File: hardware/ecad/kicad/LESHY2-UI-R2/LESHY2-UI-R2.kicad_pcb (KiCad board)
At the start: 6 copper layers, 80 x 150 mm, 432 parts, among them J1 Hirose FH34SRJ-50S-0.5SH(50), J10 Samtec FTSH-105-01-L-DV-K-P-TR, J11 GCT USB4105-GF-A, J12 GCT RFPC-SMA31-FN-175-A, J13 Hirose U.FL-R-SMT-1(80), J14 GCT RFPC-SMA31-FN-175-A, J15 Hirose U.FL-R-SMT-1(80), J16 GCT RFPC-SMA31-FN-175-A, J17 Hirose U.FL-R-SMT-1(80), J18 Hirose FX8C-80P-SV1(92), J2 Samtec FTSH-105-01-L-DV-K-P-TR, J3 GCT RFPC-SMA32-FN-175-A, J4 Hirose U.FL-R-SMT-1(80), J5 Hirose DM3AT-SF-PEJM5, J6 Samtec FTSH-105-01-L-DV-K-P-TR, J7 GCT RFPC-SMA32-FN-175-A, J8 Hirose U.FL-R-SMT-1(80), J9 GCT USB4105-GF-A, Q1 Diodes Incorporated DMN2056U-7, Q2 Diodes Incorporated 2N7002DW-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, Q3 Diodes Incorporated DMN2056U-7, Q4 Diodes Incorporated DMN2056U-7, Q5 Diodes Incorporated DMN2056U-7, Q6 Diodes Incorporated 2N7002DW-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, SW1 Alps Alpine SKRTLAE010, SW10 OMRON B3S-1100P, SW11 OMRON B3S-1100P, SW12 OMRON B3S-1100P, SW13 OMRON B3S-1100P, SW14 OMRON B3S-1100P, SW15 OMRON B3S-1100P, SW16 OMRON B3S-1100P, SW17 OMRON B3S-1100P, SW18 Alps Alpine SKRTLAE010, SW19 Alps Alpine SKRTLAE010, SW2 Alps Alpine SKRTLAE010, SW20 Alps Alpine SKRTLAE010, SW21 Alps Alpine SKRTLAE010, SW3 OMRON B3S-1100P, SW4 OMRON B3S-1100P, SW5 OMRON B3S-1100P, SW6 OMRON B3S-1100P, SW7 OMRON B3S-1100P, SW8 OMRON B3S-1100P, SW9 OMRON B3S-1100P, U1 ESP32-S3-WROOM-1U-N16R8, U10 Texas Instruments TPS22919DCKR, U11 SN74LVC1G07DCKR, U12 Texas Instruments TPD8E003DQDR, U13 TCA9539PWR, U14 ESP32-C5-WROOM-1U-N8R8, U15 Texas Instruments TPD4E05U06D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, U16 KYOCERA AVX CP0603Q5425ENTR, U17 74LVC2G14GV,125, U18 SN74LVC1G74DCUR, U19 74HC20PW,118, U2 Texas Instruments TPD4E05U06D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, U20 74LVC2G14GV,125, U21 Texas Instruments TPD2EUSB30A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, U22 onsemi FSUSB42MUX, U23 Vishay TSMP95000TT, U24 Vishay TSOP75238TR, U25 Texas Instruments TPS22919DCKR, U26 Nexperia 74LVC2G126DP,125, U27 SN74LVC1G08DCKR, U28 SC1512-A4, U29 Texas Instruments TPD4E05U06D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, U3 KYOCERA AVX CP0603Q5425ENTR, U30 Texas Instruments TPD2EUSB30A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, U31 onsemi FSUSB42MUX, U32 Analog Devices AD8314ARMZ-REEL, U33 Analog Devices AD8314ARMZ-REEL, U34 Analog Devices AD8314ARMZ-REEL, U35 Ebyte E01-ML01SP4, U36 TTM Technologies DC2337J5010A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, U37 Nexperia 74LVC126APW,118, U38 Nexperia 74LVC2G126DP,125, U39 Ebyte E01-ML01SP4, U4 Texas Instruments TPS2553DRVR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, U40 TTM Technologies DC2337J5010A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

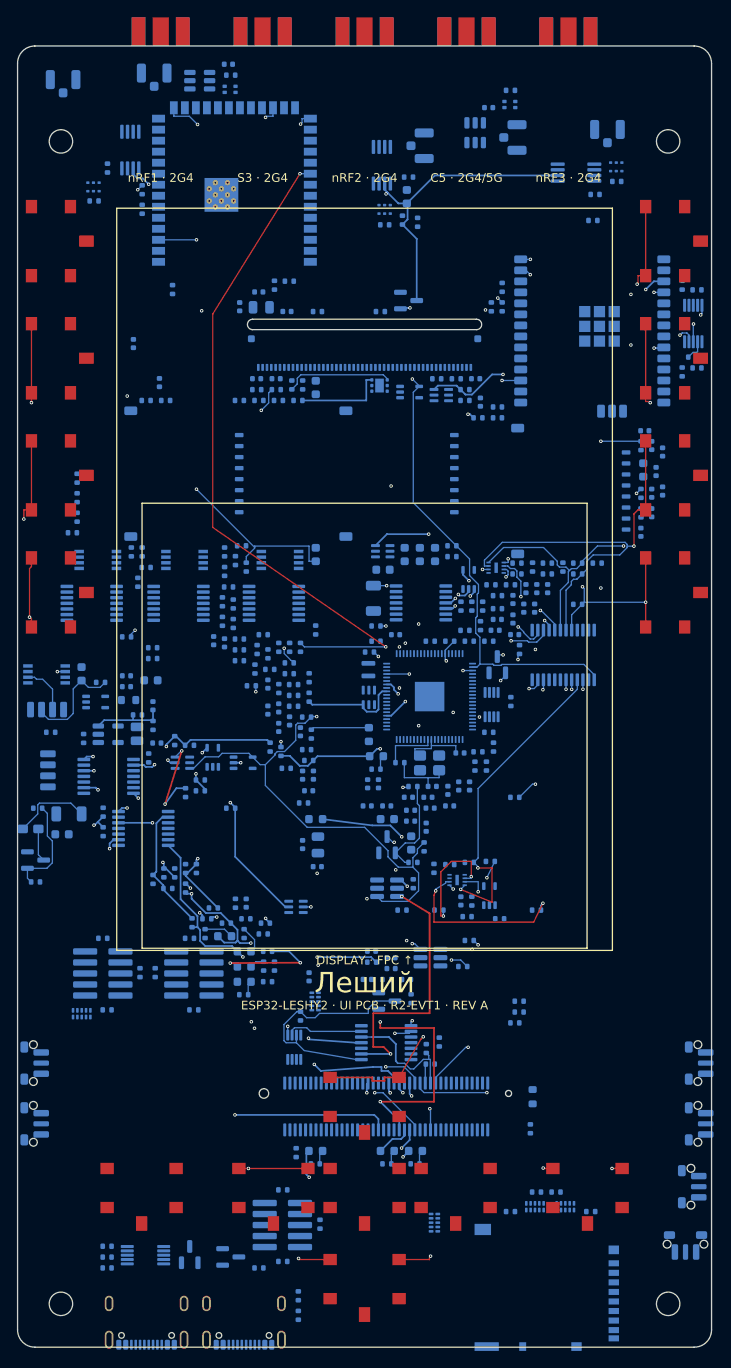
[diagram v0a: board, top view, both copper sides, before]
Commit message: Restore clean H6 analogue routing on 80 mm boards
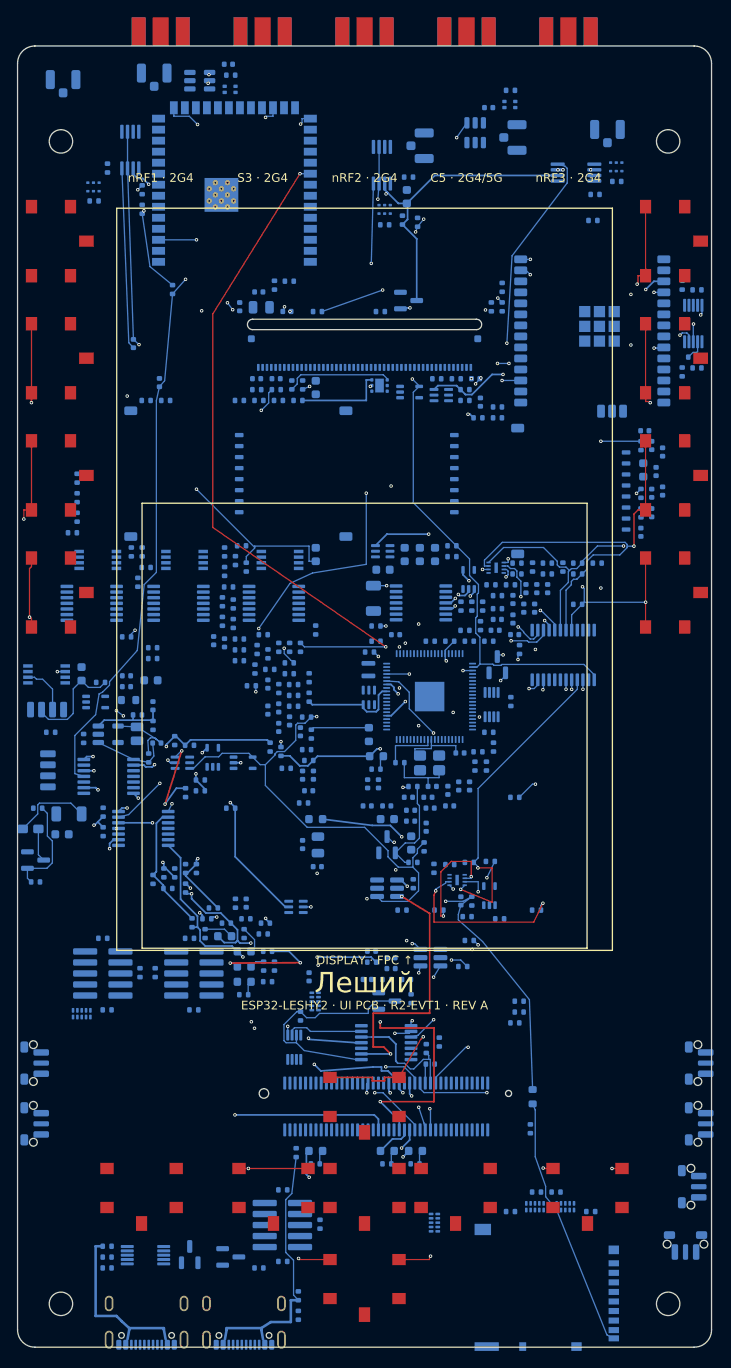
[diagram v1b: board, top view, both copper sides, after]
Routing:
- net /UI_31_NRF24_X3_TX_EVIDENCE/NRF2_DETECT_V: track 0.00 -> 97.8 mm, vias 0 -> 10
- net /UI_31_NRF24_X3_TX_EVIDENCE/NRF1_DETECT_V: track 0.00 -> 96.8 mm, vias 0 -> 5
- net /UI_10_S3_DISPLAY_TOUCH/S3_DETECT_V: track 0.00 -> 86.0 mm, vias 0 -> 2
- net /UI_31_NRF24_X3_TX_EVIDENCE/NRF0_DETECT_V: track 0.00 -> 82.4 mm, vias 0 -> 4
- net /UI_11_STORAGE_CONTROLS_INDICATORS/SD_DETECT_N: track 0.00 -> 57.7 mm, vias 0 -> 2
- net /UI_20_C5_WIFI_IR_SERVICE/C5_SERVICE_VBUS_SENSE_ONLY: track 0.00 -> 31.0 mm
- net /UI_11_STORAGE_CONTROLS_INDICATORS/SD_CARD_DETECT_RAW_N: track 0.00 -> 29.4 mm
- net /UI_31_NRF24_X3_TX_EVIDENCE/NRF2_DETECT_FILTER: track 0.00 -> 29.3 mm, vias 0 -> 2
- net /UI_20_C5_WIFI_IR_SERVICE/C5_DETECT_VM: track 0.00 -> 29.1 mm, vias 0 -> 4
- net /UI_10_S3_DISPLAY_TOUCH/S3_DETECT_VM: track 0.00 -> 27.7 mm, vias 0 -> 2
- net /UI_31_NRF24_X3_TX_EVIDENCE/NRF1_DETECT_FILTER: track 0.00 -> 21.0 mm, vias 0 -> 2
- net /UI_31_NRF24_X3_TX_EVIDENCE/NRF0_DETECT_FILTER: track 0.00 -> 20.9 mm
- net /UI_30_HUB_RP_CORE_SERVICE/HUB_RP_SERVICE_VBUS_SENSE_ONLY: track 0.00 -> 19.9 mm
- net /UI_20_C5_WIFI_IR_SERVICE/C5_SERVICE_PATH_ACK: track 0.00 -> 19.0 mm, vias 0 -> 2
- net /UI_20_C5_WIFI_IR_SERVICE/C5_SERVICE_PATH_ACK_N: track 0.00 -> 9.79 mm, vias 0 -> 2
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
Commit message: Complete UI analogue routing on H6 boards
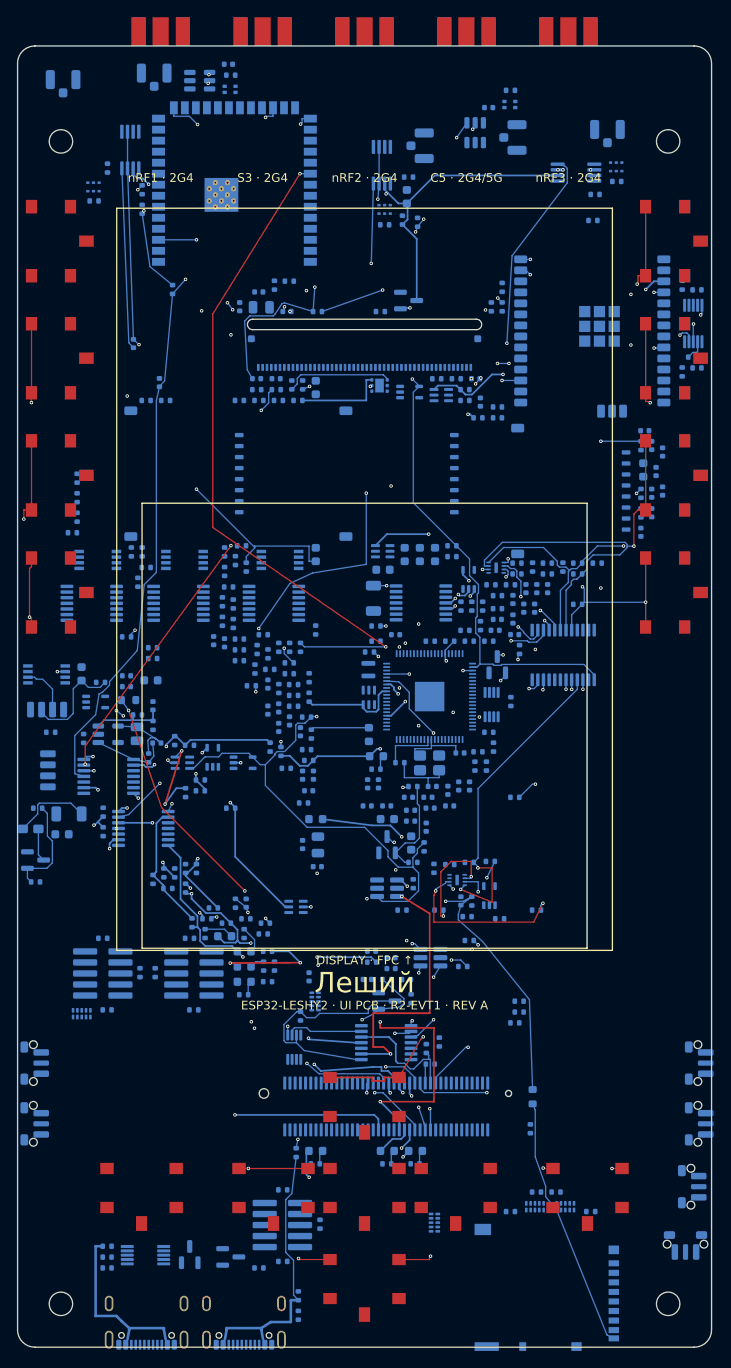
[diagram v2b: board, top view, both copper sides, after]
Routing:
- net /UI_20_C5_WIFI_IR_SERVICE/C5_DETECT_V: track 0.00 -> 111.6 mm, vias 0 -> 6
- net /UI_11_STORAGE_CONTROLS_INDICATORS/UI_ZONE_TEMP_ADC: track 0.00 -> 60.6 mm, vias 0 -> 4
- net /UI_20_C5_WIFI_IR_SERVICE/C5_SERVICE_VBUS_DIVIDED: track 0.00 -> 25.9 mm, vias 0 -> 2

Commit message: Repack boards around electrical owners
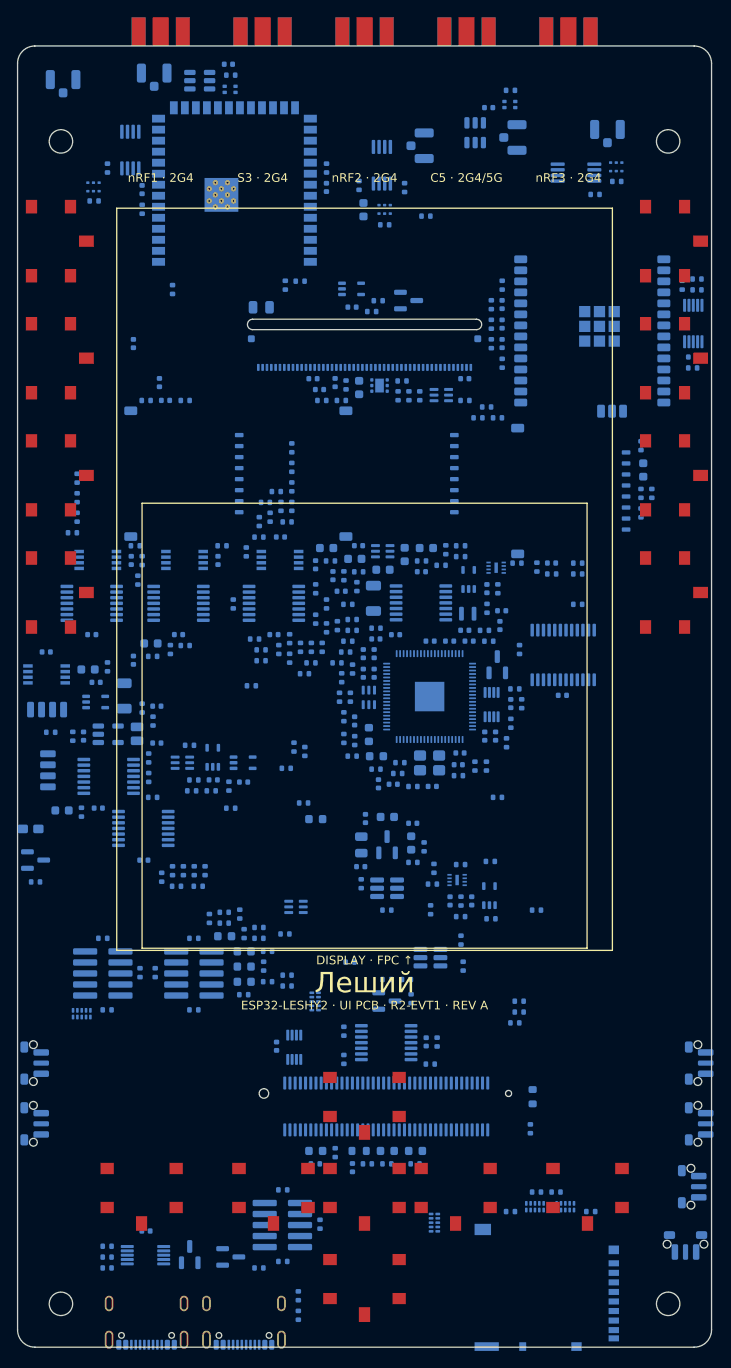
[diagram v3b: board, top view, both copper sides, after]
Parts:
- moved C25 81.6 mm to (29.9, 115.3)
- moved C31 74.4 mm to (7.61, 79.6)
- moved C26 70.9 mm to (47.1, 114.8)
- moved C37 68.9 mm to (9.05, 73.4), turned to 0 degrees
- moved R73 58.4 mm to (39.4, 127.4)
- moved C18 57.5 mm to (38.6, 30.1)
- moved C54 55.6 mm to (14.8, 136.6), turned to 0 degrees
- moved C61 48.7 mm to (8.55, 67.9), turned to 0 degrees
- moved C59 45.8 mm to (17.1, 40.9)
- moved C64 44.5 mm to (13.1, 59.3)
- moved C85 44.1 mm to (46.6, 60.6)
- moved C67 43.9 mm to (18.6, 67.9), turned to 0 degrees
- moved C80 38.5 mm to (9.30, 87.9)
- moved R74 33.7 mm to (40.3, 128.9), turned to 0 degrees
- moved C20 32.9 mm to (38.6, 129.3)
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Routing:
- net /UI_20_C5_WIFI_IR_SERVICE/EV_N7_IR: track 169.1 -> 0.00 mm, vias 6 -> 0
- net /UI_10_S3_DISPLAY_TOUCH/S3_RESET_N: track 147.0 -> 0.00 mm, vias 5 -> 0
- net /UI_10_S3_DISPLAY_TOUCH/ENCODER_B: track 134.9 -> 0.00 mm, vias 3 -> 0
- net /UI_10_S3_DISPLAY_TOUCH/ENCODER_A: track 132.0 -> 0.00 mm, vias 3 -> 0
- net /UI_20_C5_WIFI_IR_SERVICE/C5_RESET_N: track 116.8 -> 0.00 mm, vias 4 -> 0
- net /UI_20_C5_WIFI_IR_SERVICE/C5_DETECT_V: track 111.6 -> 0.00 mm, vias 6 -> 0
- net /UI_11_STORAGE_CONTROLS_INDICATORS/UI_F3_N: track 106.9 -> 0.00 mm, vias 5 -> 0
- net /UI_11_STORAGE_CONTROLS_INDICATORS/UI_DPAD_DOWN_N: track 105.7 -> 0.00 mm, vias 5 -> 0
- net /UI_10_S3_DISPLAY_TOUCH/UI_HUB_ALERT_N: track 105.6 -> 0.00 mm, vias 3 -> 0
- net /UI_31_NRF24_X3_TX_EVIDENCE/FAULT_ASSERT_N: track 101.4 -> 0.00 mm, vias 5 -> 0
- net /UI_11_STORAGE_CONTROLS_INDICATORS/UI_DPAD_LEFT_N: track 101.2 -> 0.00 mm, vias 4 -> 0
- net /UI_31_NRF24_X3_TX_EVIDENCE/NRF2_DETECT_V: track 97.8 -> 0.00 mm, vias 10 -> 0
- net /UI_31_NRF24_X3_TX_EVIDENCE/NRF1_DETECT_V: track 96.8 -> 0.00 mm, vias 5 -> 0
- net /UI_20_C5_WIFI_IR_SERVICE/C5_MUX_DISABLE: track 90.7 -> 0.00 mm, vias 4 -> 0
- net /UI_11_STORAGE_CONTROLS_INDICATORS/UI_F2_N: track 88.6 -> 0.00 mm, vias 4 -> 0
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
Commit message: Add direct battery cell thermal contacts
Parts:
- removed the C17 at (42.6, 88.9)
- removed the C23 at (34.8, 39.6)
- removed the C26 at (47.1, 114.8)
- removed the C31 at (7.61, 79.6)
- removed the C80 at (9.30, 87.9)
- removed the C9 at (36.6, 38.8)
- removed the J3 at (28.2, 0.00)
- removed the J7 at (51.8, 0.00)
- removed the R102 at (77.8, 37.1)
- removed the R127 at (36.1, 59.4)
- removed the R146 at (13.6, 57.6)
- removed the R149 at (10.4, 14.1)
- removed the R173 at (37.4, 72.8)
- removed the R180 at (29.1, 54.3)
- removed the R207 at (51.6, 40.9)
- removed the R216 at (17.9, 95.1)
- removed the R36 at (26.1, 109.4)
- removed the R41 at (66.1, 134.4)
- removed the R61 at (39.3, 60.6)
- removed the R86 at (31.9, 80.8)
- removed the R90 at (76.6, 27.6)
- removed the SW12 at (4.77, 63.0)
- removed the SW14 at (75.6, 36.0)
- removed the SW17 at (65.7, 132.6)
- removed the SW9 at (4.77, 22.5)
- removed the U30 at (19.8, 139.3)
- removed the U32 at (13.0, 12.0)
- removed the U33 at (42.0, 13.8)
- removed the U40 at (42.3, 18.8)
- removed the U41 at (18.6, 64.2)
- added C3: KEMET C0402C330J5GACTU, Capacitor_SMD:C_0402_1005Metric, B.Cu at (16.4, 38.8)
- added C41: Yageo CC0402KRX7R9BB104, Capacitor_SMD:C_0402_1005Metric, B.Cu at (47.6, 68.6)
- added C54: Yageo CC0402KRX7R9BB104, Capacitor_SMD:C_0402_1005Metric, B.Cu at (14.8, 136.6)
- added C57: TDK C1005X5R0J475K050BC, Capacitor_SMD:C_0402_1005Metric, B.Cu at (55.8, 65.1)
- added D8: LTST-C190KRKT, LED_SMD:LED_0603_1608Metric, B.Cu at (26.1, 104.4)
- added J16: GCT RFPC-SMA31-FN-175-A, Leshy2:RFPC-SMA31-FN-175-A, F.Cu at (63.5, 0.00)
- added J2: Samtec FTSH-105-01-L-DV-K-P-TR, Leshy2:FTSH-105-01-L-DV-K-P-TR, B.Cu at (9.82, 106.9)
- added MH1: M2.5 compression-stop axis, MountingHole_2.7mm_M2.5, F.Cu at (5.00, 11.0)
- added MH2: M2.5 compression-stop axis, MountingHole_2.7mm_M2.5, F.Cu at (75.0, 11.0)
- added R107: Yageo RC0402FR-075K1L, Resistor_SMD:R_0402_1005Metric, B.Cu at (32.4, 146.3)
- added R114: Yageo RC0402FR-0710KL, Resistor_SMD:R_0402_1005Metric, B.Cu at (54.6, 29.8)
- added R135: Yageo RC0402FR-0710KL, Resistor_SMD:R_0402_1005Metric, B.Cu at (30.6, 131.9)
- added R145: Yageo RC0402FR-0733RL, Resistor_SMD:R_0402_1005Metric, B.Cu at (43.8, 83.9)
- added R160: Yageo RC0402FR-0710KL, Resistor_SMD:R_0402_1005Metric, B.Cu at (6.86, 54.3)
- added R177: Panasonic ERJ-2RKF22R0X, Resistor_SMD:R_0402_1005Metric, B.Cu at (35.6, 67.1)
- added R193: Yageo RC0402FR-0710KL, Resistor_SMD:R_0402_1005Metric, B.Cu at (58.1, 75.8)
- added R204: Panasonic ERJ-2RKF22R0X, Resistor_SMD:R_0402_1005Metric, B.Cu at (55.4, 62.6)
- added R21: UNI-ROYAL 0402WGF1333TCE, Resistor_SMD:R_0402_1005Metric, B.Cu at (44.3, 38.6)
- added R47: Yageo RC0603FR-071KL, Resistor_SMD:R_0603_1608Metric, B.Cu at (59.4, 121.1)
- added R52: Panasonic ERJ-2RKF22R0X, Resistor_SMD:R_0402_1005Metric, B.Cu at (54.0, 83.0)
- added R64: Yageo RC0402FR-073K32L, Resistor_SMD:R_0402_1005Metric, B.Cu at (71.9, 51.6)
- added R72: Yageo RC0402FR-0710KL, Resistor_SMD:R_0402_1005Metric, B.Cu at (51.1, 94.4)
- added R81: Yageo RC0402FR-0710KL, Resistor_SMD:R_0402_1005Metric, B.Cu at (20.3, 111.1)
- added SW6: OMRON B3S-1100P, Leshy2:B3S-1100P, F.Cu at (50.5, 132.6)
- added SW7: OMRON B3S-1100P, Leshy2:B3S-1100P, F.Cu at (40.0, 122.1)
- added SW8: OMRON B3S-1100P, Leshy2:B3S-1100P, F.Cu at (14.3, 132.6)
- added U15: Texas Instruments TPD4E05U06DQAR, Package_SON:USON-10_2.5x1.0mm_P0.5mm, B.Cu at (34.3, 110.1)
- added U19: 74HC20PW,118, Package_SO:TSSOP-14_4.4x5mm_P0.65mm, B.Cu at (42.5, 114.9)
- added U2: Texas Instruments TPD4E05U06DQAR, Package_SON:USON-10_2.5x1.0mm_P0.5mm, B.Cu at (7.39, 111.6)
- added U46: Nexperia 74LVC2G126DP,125, Package_SO:TSSOP-8_3x3mm_P0.65mm, B.Cu at (30.2, 59.2)
- C17: renamed from D8; value LTST-C190KRKT -> TDK C1608X7R1C105K080AC; footprint LED_SMD:LED_0603_1608Metric -> Capacitor_SMD:C_0603_1608Metric
- C23: renamed from R64; value Yageo RC0402FR-073K32L -> KEMET C0402C330J5GACTU; footprint Resistor_SMD:R_0402_1005Metric -> Capacitor_SMD:C_0402_1005Metric
- C26: renamed from U2; value Texas Instruments TPD4E05U06DQAR -> Yageo CC0402KRX7R9BB104; footprint Package_SON:USON-10_2.5x1.0mm_P0.5mm -> Capacitor_SMD:C_0402_1005Metric
- C31: renamed from R21; value UNI-ROYAL 0402WGF1333TCE -> Yageo CC0402KRX7R9BB104; footprint Resistor_SMD:R_0402_1005Metric -> Capacitor_SMD:C_0402_1005Metric
- C80: renamed from C3; value KEMET C0402C330J5GACTU -> Yageo CC0402KRX7R9BB104
- C9: renamed from U46; value Nexperia 74LVC2G126DP,125 -> Yageo CC0402KRX7R9BB104; footprint Package_SO:TSSOP-8_3x3mm_P0.65mm -> Capacitor_SMD:C_0402_1005Metric
- J12: renamed from SW11; value OMRON B3S-1100P -> GCT RFPC-SMA31-FN-175-A; footprint Leshy2:B3S-1100P -> Leshy2:RFPC-SMA31-FN-175-A
- J14: renamed from SW6; value OMRON B3S-1100P -> GCT RFPC-SMA31-FN-175-A; footprint Leshy2:B3S-1100P -> Leshy2:RFPC-SMA31-FN-175-A
- J3: renamed from MH1; value M2.5 compression-stop axis -> GCT RFPC-SMA32-FN-175-A; footprint MountingHole_2.7mm_M2.5 -> Leshy2:RFPC-SMA32-FN-175-A
- J7: renamed from J12; value GCT RFPC-SMA31-FN-175-A -> GCT RFPC-SMA32-FN-175-A; footprint Leshy2:RFPC-SMA31-FN-175-A -> Leshy2:RFPC-SMA32-FN-175-A
- R127: renamed from R107; value Yageo RC0402FR-075K1L -> Yageo RC0402FR-0710KL
- R149: renamed from R193; value Yageo RC0402FR-0710KL -> Yageo RC0402FR-0752R3L
- R175: renamed from U15; value Texas Instruments TPD4E05U06DQAR -> Yageo RC0402FR-0710KL; footprint Package_SON:USON-10_2.5x1.0mm_P0.5mm -> Resistor_SMD:R_0402_1005Metric
- R180: renamed from C57; value TDK C1005X5R0J475K050BC -> Yageo RC0402FR-0710KL; footprint Capacitor_SMD:C_0402_1005Metric -> Resistor_SMD:R_0402_1005Metric
- R216: renamed from U19; value 74HC20PW,118 -> Yageo RC0402FR-07100KL; footprint Package_SO:TSSOP-14_4.4x5mm_P0.65mm -> Resistor_SMD:R_0402_1005Metric
- R36: renamed from R204; value Panasonic ERJ-2RKF22R0X -> UNI-ROYAL 0402WGF2201TCE
- R41: renamed from C54; value Yageo CC0402KRX7R9BB104 -> Yageo RC0402FR-0710KL; footprint Capacitor_SMD:C_0402_1005Metric -> Resistor_SMD:R_0402_1005Metric
- R61: renamed from R145; value Yageo RC0402FR-0733RL -> Yageo RC0402FR-073K32L
- R86: renamed from C41; value Yageo CC0402KRX7R9BB104 -> Yageo RC0402FR-071ML; footprint Capacitor_SMD:C_0402_1005Metric -> Resistor_SMD:R_0402_1005Metric
- R90: renamed from J2; value Samtec FTSH-105-01-L-DV-K-P-TR -> Yageo RC0402FR-0710KL; footprint Leshy2:FTSH-105-01-L-DV-K-P-TR -> Resistor_SMD:R_0402_1005Metric
- SW10: renamed from J16; value GCT RFPC-SMA31-FN-175-A -> OMRON B3S-1100P; footprint Leshy2:RFPC-SMA31-FN-175-A -> Leshy2:B3S-1100P
- SW11: renamed from MH2; value M2.5 compression-stop axis -> OMRON B3S-1100P; footprint MountingHole_2.7mm_M2.5 -> Leshy2:B3S-1100P
- SW17: renamed from J14; value GCT RFPC-SMA31-FN-175-A -> OMRON B3S-1100P; footprint Leshy2:RFPC-SMA31-FN-175-A -> Leshy2:B3S-1100P
- U30: renamed from R175; value Yageo RC0402FR-0710KL -> Texas Instruments TPD2EUSB30ADRTR; footprint Resistor_SMD:R_0402_1005Metric -> Package_TO_SOT_SMD:SOT-23
- U32: renamed from R47; value Yageo RC0603FR-071KL -> Analog Devices AD8314ARMZ-REEL; footprint Resistor_SMD:R_0603_1608Metric -> Package_SO:MSOP-8_3x3mm_P0.65mm
- U33: renamed from R135; value Yageo RC0402FR-0710KL -> Analog Devices AD8314ARMZ-REEL; footprint Resistor_SMD:R_0402_1005Metric -> Package_SO:MSOP-8_3x3mm_P0.65mm
- U40: renamed from R177; value Panasonic ERJ-2RKF22R0X -> TTM Technologies DC2337J5010AHF; footprint Resistor_SMD:R_0402_1005Metric -> Leshy2:DC2337J5010AHF
- U41: renamed from R114; value Yageo RC0402FR-0710KL -> Nexperia 74LVC126APW,118; footprint Resistor_SMD:R_0402_1005Metric -> Package_SO:TSSOP-14_4.4x5mm_P0.65mm
- moved SW17 135.0 mm to (65.7, 132.6)
- moved J14 133.0 mm to (40.0, 0.00)
- moved SW13 119.3 mm to (75.6, 22.5), turned to 90 degrees
- moved U33 118.7 mm to (42.0, 13.8), turned to 90 degrees
- moved U32 118.6 mm to (13.0, 12.0)
- moved SW5 115.7 mm to (40.0, 132.6), turned to 0 degrees
- moved SW9 115.6 mm to (4.77, 22.5), turned to 90 degrees
- moved R90 103.7 mm to (76.6, 27.6)
- moved SW15 100.1 mm to (75.6, 49.5), turned to 90 degrees
- moved R127 87.0 mm to (36.1, 59.4), turned to 0 degrees
- moved SW11 80.1 mm to (4.77, 49.5), turned to 90 degrees
- moved R149 78.1 mm to (10.4, 14.1)
- moved R102 73.0 mm to (77.8, 37.1), turned to 0 degrees
- moved SW12 72.1 mm to (4.77, 63.0)
- moved SW14 70.8 mm to (75.6, 36.0)
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- renumbered R160 to R102, R52 to R146, R81 to R173, R72 to R207, SW15 to SW12, SW4 to SW13, SW10 to SW14, SW3 to SW15, SW8 to SW3, SW7 to SW4, SW13 to SW5, SW5 to SW9
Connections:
- C17 pad 1: /UI_50_FRONT_POWER_SAFETY/EV_N4_NRF2 -> /UI_10_S3_DISPLAY_TOUCH/3V3_MAIN
- C17 pad 2: /UI_11_STORAGE_CONTROLS_INDICATORS/NRF2_TX_LED_A -> /UI_10_S3_DISPLAY_TOUCH/POWER_GROUND
- C23 pad 1: /UI_10_S3_DISPLAY_TOUCH/3V3_MAIN -> /UI_20_C5_WIFI_IR_SERVICE/C5_DETECT_V
- C23 pad 2: /UI_11_STORAGE_CONTROLS_INDICATORS/UI_F5_N -> /UI_10_S3_DISPLAY_TOUCH/POWER_GROUND
- C26 pad 1: /UI_10_S3_DISPLAY_TOUCH/S3_DBG_RESET_CONNECTOR_N -> /UI_10_S3_DISPLAY_TOUCH/AON_SAFE_3V3
- C26 pad 2: /UI_10_S3_DISPLAY_TOUCH/S3_DBG_BOOT_CONNECTOR_N -> /UI_10_S3_DISPLAY_TOUCH/POWER_GROUND
- C31 pad 1: /UI_11_STORAGE_CONTROLS_INDICATORS/LCD_BACKLIGHT_ILIM -> /UI_10_S3_DISPLAY_TOUCH/AON_SAFE_3V3
- C80 pad 1: /UI_10_S3_DISPLAY_TOUCH/S3_DETECT_V -> /UI_10_S3_DISPLAY_TOUCH/AON_SAFE_3V3
- C9 pad 1: /UI_31_NRF24_X3_TX_EVIDENCE/3V3_NRF_GROUP -> /UI_11_STORAGE_CONTROLS_INDICATORS/LCD_LEDA_PROTECTED
- C9 pad 2: /UI_31_NRF24_X3_TX_EVIDENCE/NRF2_MISO_MODULE -> /UI_10_S3_DISPLAY_TOUCH/POWER_GROUND
- J12 pad 1: /UI_11_STORAGE_CONTROLS_INDICATORS/UI_F3_N -> /UI_31_NRF24_X3_TX_EVIDENCE/NRF0_EXTERNAL_RF_50R
- J12 pad 3: /UI_11_STORAGE_CONTROLS_INDICATORS/UI_F3_N -> /UI_10_S3_DISPLAY_TOUCH/POWER_GROUND
- J14 pad 1: /UI_11_STORAGE_CONTROLS_INDICATORS/UI_DPAD_RIGHT_N -> /UI_31_NRF24_X3_TX_EVIDENCE/NRF1_EXTERNAL_RF_50R
- J14 pad 3: /UI_11_STORAGE_CONTROLS_INDICATORS/UI_DPAD_RIGHT_N -> /UI_10_S3_DISPLAY_TOUCH/POWER_GROUND
- J7 pad 1: /UI_31_NRF24_X3_TX_EVIDENCE/NRF0_EXTERNAL_RF_50R -> /UI_20_C5_WIFI_IR_SERVICE/C5_EXTERNAL_RF_50R
- R102 pad 1: /UI_31_NRF24_X3_TX_EVIDENCE/NRF0_IRQ_MODULE_N -> /UI_10_S3_DISPLAY_TOUCH/3V3_MAIN
- R102 pad 2: /UI_31_NRF24_X3_TX_EVIDENCE/3V3_NRF_GROUP -> /UI_20_C5_WIFI_IR_SERVICE/HUB_C5_SDIO_DAT2_BRANCH
- R127 pad 1: /UI_20_C5_WIFI_IR_SERVICE/C5_SERVICE_CC2 -> /UI_20_C5_WIFI_IR_SERVICE/IR_TX_CARRIER
- R146 pad 1: /UI_11_STORAGE_CONTROLS_INDICATORS/SD_MISO_BUFFERED -> /UI_31_NRF24_X3_TX_EVIDENCE/NRF0_CE_BUFFERED
- R146 pad 2: /UI_11_STORAGE_CONTROLS_INDICATORS/SD_MISO -> /UI_31_NRF24_X3_TX_EVIDENCE/NRF0_CE_MODULE
- R149 pad 1: /UI_31_NRF24_X3_TX_EVIDENCE/NRF2_MISO -> /UI_31_NRF24_X3_TX_EVIDENCE/NRF0_FORWARD_RF_SAMPLE
- R173 pad 1: /UI_20_C5_WIFI_IR_SERVICE/C5_DBG_ID1 -> /UI_31_NRF24_X3_TX_EVIDENCE/NRF1_MISO
- R175 pad 1: /UI_20_C5_WIFI_IR_SERVICE/C5_DBG_RESET_CONNECTOR_N -> /UI_31_NRF24_X3_TX_EVIDENCE/NRF1_SCK
- R175 pad 2: /UI_20_C5_WIFI_IR_SERVICE/C5_DBG_BOOT_CONNECTOR_N -> /UI_10_S3_DISPLAY_TOUCH/POWER_GROUND
- R180 pad 1: /UI_30_HUB_RP_CORE_SERVICE/HUB_RP_CORE_1V1 -> /UI_31_NRF24_X3_TX_EVIDENCE/NRF1_IRQ_MODULE_N
- R180 pad 2: /UI_10_S3_DISPLAY_TOUCH/POWER_GROUND -> /UI_31_NRF24_X3_TX_EVIDENCE/3V3_NRF_GROUP
- R207 pad 1: /UI_10_S3_DISPLAY_TOUCH/3V3_MAIN -> /UI_31_NRF24_X3_TX_EVIDENCE/NRF_GROUP_PWR_EN_SAFE
- R207 pad 2: /UI_11_STORAGE_CONTROLS_INDICATORS/UI_DPAD_UP_N -> /UI_10_S3_DISPLAY_TOUCH/POWER_GROUND
- R216 pad 1: /UI_20_C5_WIFI_IR_SERVICE/SERVICE_VBUS_PRESENT_N -> /UI_10_S3_DISPLAY_TOUCH/AON_SAFE_3V3
- R216 pad 2: /UI_20_C5_WIFI_IR_SERVICE/C5_EN_LOW_PROOF -> /UI_50_FRONT_POWER_SAFETY/EV_THRESH_2_NRF0
- R36 pad 1: /UI_31_NRF24_X3_TX_EVIDENCE/NRF2_MOSI_BUFFERED -> /UI_10_S3_DISPLAY_TOUCH/AON_SAFE_3V3
- R36 pad 2: /UI_31_NRF24_X3_TX_EVIDENCE/NRF2_MOSI_MODULE -> /UI_11_STORAGE_CONTROLS_INDICATORS/NRF1_TX_LED_A
- R41 pad 1: /UI_10_S3_DISPLAY_TOUCH/3V3_MAIN -> /UI_11_STORAGE_CONTROLS_INDICATORS/SD_CARD_3V3
- R41 pad 2: /UI_10_S3_DISPLAY_TOUCH/POWER_GROUND -> /UI_11_STORAGE_CONTROLS_INDICATORS/SD_DAT1_PROTECTED
- R61 pad 2: /UI_30_HUB_RP_CORE_SERVICE/HUB_RP_VREG_AVDD_FILTERED -> /UI_11_STORAGE_CONTROLS_INDICATORS/UI_F2_N
- R86 pad 1: /UI_30_HUB_RP_CORE_SERVICE/HUB_RP_CORE_1V1 -> /UI_20_C5_WIFI_IR_SERVICE/EV_N1_C5
- R86 pad 2: /UI_10_S3_DISPLAY_TOUCH/POWER_GROUND -> /UI_20_C5_WIFI_IR_SERVICE/EV_THRESH_1_C5
- R90 pad 1: /UI_10_S3_DISPLAY_TOUCH/S3_DBG_VTREF_SENSE -> /UI_10_S3_DISPLAY_TOUCH/3V3_MAIN
- R90 pad 2: /UI_10_S3_DISPLAY_TOUCH/POWER_GROUND -> /UI_20_C5_WIFI_IR_SERVICE/C5_GPIO27_FIXED_HIGH
- SW10 pad 1: /UI_31_NRF24_X3_TX_EVIDENCE/NRF2_EXTERNAL_RF_50R -> /UI_11_STORAGE_CONTROLS_INDICATORS/UI_F2_N
- SW10 pad 3: /UI_10_S3_DISPLAY_TOUCH/POWER_GROUND -> /UI_11_STORAGE_CONTROLS_INDICATORS/UI_F2_N
- SW12 pad 1: /UI_11_STORAGE_CONTROLS_INDICATORS/UI_F7_N -> /UI_11_STORAGE_CONTROLS_INDICATORS/UI_F4_N
- SW12 pad 3: /UI_11_STORAGE_CONTROLS_INDICATORS/UI_F7_N -> /UI_11_STORAGE_CONTROLS_INDICATORS/UI_F4_N
- SW13 pad 1: /UI_11_STORAGE_CONTROLS_INDICATORS/UI_DPAD_LEFT_N -> /UI_11_STORAGE_CONTROLS_INDICATORS/UI_F5_N
- SW13 pad 3: /UI_11_STORAGE_CONTROLS_INDICATORS/UI_DPAD_LEFT_N -> /UI_11_STORAGE_CONTROLS_INDICATORS/UI_F5_N
- SW14 pad 1: /UI_11_STORAGE_CONTROLS_INDICATORS/UI_F2_N -> /UI_11_STORAGE_CONTROLS_INDICATORS/UI_F6_N
- SW14 pad 3: /UI_11_STORAGE_CONTROLS_INDICATORS/UI_F2_N -> /UI_11_STORAGE_CONTROLS_INDICATORS/UI_F6_N
- SW15 pad 1: /UI_11_STORAGE_CONTROLS_INDICATORS/UI_DPAD_DOWN_N -> /UI_11_STORAGE_CONTROLS_INDICATORS/UI_F7_N
- SW15 pad 3: /UI_11_STORAGE_CONTROLS_INDICATORS/UI_DPAD_DOWN_N -> /UI_11_STORAGE_CONTROLS_INDICATORS/UI_F7_N
- SW17 pad 1: /UI_31_NRF24_X3_TX_EVIDENCE/NRF1_EXTERNAL_RF_50R -> /UI_11_STORAGE_CONTROLS_INDICATORS/UI_OPT_N
- SW17 pad 3: /UI_10_S3_DISPLAY_TOUCH/POWER_GROUND -> /UI_11_STORAGE_CONTROLS_INDICATORS/UI_OPT_N
- SW3 pad 1: /UI_11_STORAGE_CONTROLS_INDICATORS/UI_BACK_N -> /UI_11_STORAGE_CONTROLS_INDICATORS/UI_DPAD_DOWN_N
- SW3 pad 3: /UI_11_STORAGE_CONTROLS_INDICATORS/UI_BACK_N -> /UI_11_STORAGE_CONTROLS_INDICATORS/UI_DPAD_DOWN_N
- SW4 pad 1: /UI_11_STORAGE_CONTROLS_INDICATORS/UI_DPAD_UP_N -> /UI_11_STORAGE_CONTROLS_INDICATORS/UI_DPAD_LEFT_N
- SW4 pad 3: /UI_11_STORAGE_CONTROLS_INDICATORS/UI_DPAD_UP_N -> /UI_11_STORAGE_CONTROLS_INDICATORS/UI_DPAD_LEFT_N
- SW5 pad 1: /UI_11_STORAGE_CONTROLS_INDICATORS/UI_F5_N -> /UI_11_STORAGE_CONTROLS_INDICATORS/UI_DPAD_OK_N
- SW5 pad 3: /UI_11_STORAGE_CONTROLS_INDICATORS/UI_F5_N -> /UI_11_STORAGE_CONTROLS_INDICATORS/UI_DPAD_OK_N
- SW9 pad 1: /UI_11_STORAGE_CONTROLS_INDICATORS/UI_DPAD_OK_N -> /UI_11_STORAGE_CONTROLS_INDICATORS/UI_F1_N
- SW9 pad 3: /UI_11_STORAGE_CONTROLS_INDICATORS/UI_DPAD_OK_N -> /UI_11_STORAGE_CONTROLS_INDICATORS/UI_F1_N
- U30 pad 1: /UI_31_NRF24_X3_TX_EVIDENCE/NRF1_SCK -> /UI_30_HUB_RP_CORE_SERVICE/HUB_RP_SERVICE_USB_CONNECTOR_P
- U30 pad 2: /UI_10_S3_DISPLAY_TOUCH/POWER_GROUND -> /UI_30_HUB_RP_CORE_SERVICE/HUB_RP_SERVICE_USB_CONNECTOR_N
- U32 pad 1: /UI_11_STORAGE_CONTROLS_INDICATORS/SD_CARD_DETECT_RAW_N -> /UI_31_NRF24_X3_TX_EVIDENCE/NRF0_FORWARD_RF_SAMPLE
- U32 pad 2: /UI_11_STORAGE_CONTROLS_INDICATORS/SD_DETECT_N -> /UI_31_NRF24_X3_TX_EVIDENCE/NRF_EVIDENCE_HOLD
- U33 pad 1: /UI_30_HUB_RP_CORE_SERVICE/HUB_RP_DBG_ID0 -> /UI_31_NRF24_X3_TX_EVIDENCE/NRF1_FORWARD_RF_SAMPLE
- U33 pad 2: /UI_10_S3_DISPLAY_TOUCH/POWER_GROUND -> /UI_31_NRF24_X3_TX_EVIDENCE/NRF_EVIDENCE_HOLD
- U40 pad 1: /UI_31_NRF24_X3_TX_EVIDENCE/NRF1_MISO_BUFFERED -> /UI_31_NRF24_X3_TX_EVIDENCE/NRF1_MODULE_RF_50R
- U40 pad 2: /UI_31_NRF24_X3_TX_EVIDENCE/NRF1_MISO -> /UI_31_NRF24_X3_TX_EVIDENCE/NRF1_FORWARD_RF_SAMPLE
- U41 pad 1: /UI_20_C5_WIFI_IR_SERVICE/IR_RX_CARRIER -> /UI_31_NRF24_X3_TX_EVIDENCE/3V3_NRF_GROUP
- U41 pad 2: /UI_10_S3_DISPLAY_TOUCH/3V3_MAIN -> /UI_31_NRF24_X3_TX_EVIDENCE/NRF1_CE_SAFE
